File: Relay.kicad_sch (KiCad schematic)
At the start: 6 parts, among them K1 Relay_SPST-NO, Q1 AO3400A

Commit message: more schematic work and initial layout
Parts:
- removed D16: D_Schottky, Diode_SMD:D_SMA, symbol Device:D_Schottky
- removed K1: Relay_SPST-NO, Relay_THT:Relay_SPST_SANYOU_SRD_Series_Form_A, symbol Relay:Relay_SPST-NO
- added D18: D_Schottky, Diode_SMD:D_SOD-123F, symbol Device:D_Schottky
- added K2: SANYOU_SRD_Form_A, Relay_THT:Relay_SPST_SANYOU_SRD_Series_Form_A, symbol Relay:SANYOU_SRD_Form_A
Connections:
- net +5V: now also D18.1 (K), K2.2
- net SW1: now also K2.3
- net SW2: now also K2.1
- net at Q1.3 (D): now also D18.2 (A), K2.5
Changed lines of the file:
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@@
 	(paper "A4")
+	(junction
+		(at 139.7 101.6)
+		(diameter 0)
+		(color 0 0 0 0)
+	)
 	(junction
 		(at 110.49 124.46)
@@
 	)
 	(junction
-		(at 154.94 101.6)
-		(diameter 0)
-		(color 0 0 0 0)
-	)
-	(junction
 		(at 121.92 124.46)
 		(diameter 0)
@@
 	)
 	(junction
-		(at 110.49 109.22)
+		(at 154.94 101.6)
 		(diameter 0)
 		(color 0 0 0 0)
 	)
 	(junction
-		(at 139.7 101.6)
+		(at 110.49 109.22)
 		(diameter 0)
 		(color 0 0 0 0)
@@
 	(hierarchical_label "SW1"
 		(shape passive)
-		(at 139.7 88.9 180)
+		(at 139.7 91.44 180)
 		(effects
 			(font
@@
 		)
 		(instances
-			(project "RSC-LV3-BPS"
+			(project "RSC-LV3-LVBPS"
 				(path "/4bbf2fff-9f66-421d-84bf-68d1dcd1e11d/99b902d4-84f6-4664-999c-14b01031412b"
 					(reference "D23")
@@
 		)
 		(instances
-			(project "RSC-LV3-BPS"
+			(project "RSC-LV3-LVBPS"
 				(path "/4bbf2fff-9f66-421d-84bf-68d1dcd1e11d/99b902d4-84f6-4664-999c-14b01031412b"
 					(reference "R29")
@@
 				(path "/4bbf2fff-9f66-421d-84bf-68d1dcd1e11d/df7bcb64-4221-4af7-8ca5-3f00264c9667"
 					(reference "R28")
-					(unit 1)
-				)
-			)
-		)
-	)
-	(symbol
-		(lib_id "Relay:Relay_SPST-NO")
-		(at 147.32 96.52 90)
-		(unit 1)
-		(body_style 1)
-		(exclude_from_sim no)
-		(in_bom yes)
-		(on_board yes)
-		(in_pos_files yes)
-		(dnp no)
-		(fields_autoplaced yes)
-		(property "Reference" "K1"
-			(at 147.32 81.28 90)
-			(show_name no)
-			(do_not_autoplace no)
-			(effects
-				(font
-					(size 1.27 1.27)
-				)
-			)
-		)
-		(property "Value" "Relay_SPST-NO"
-			(at 147.32 83.82 90)
-			(show_name no)
-			(do_not_autoplace no)
-			(effects
-				(font
-					(size 1.27 1.27)
-				)
-			)
-		)
-		(property "Footprint" "Relay_THT:Relay_SPST_SANYOU_SRD_Series_Form_A"
-			(at 148.59 85.09 0)
-			(hide yes)
-			(show_name no)
-			(do_not_autoplace no)
-			(effects
-				(font
-					(size 1.27 1.27)
-				)
-				(justify left)
-			)
-		)
-		(property "Datasheet" ""
-			(at 147.32 96.52 0)
-			(hide yes)
-			(show_name no)
-			(do_not_autoplace no)
-			(effects
-				(font
-					(size 1.27 1.27)
-				)
-			)
-		)
-		(property "Description" "Relay SPST, normally open, EN50005"
-			(at 147.32 96.52 0)
-			(hide yes)
-			(show_name no)
-			(do_not_autoplace no)
-			(effects
-				(font
-					(size 1.27 1.27)
-				)
-			)
-		)
-		(pin "A2"
-		)
-		(pin "A1"
-		)
-		(pin "14"
-		)
-		(pin "13"
-		)
-		(instances
-			(project "RSC-LV3-BPS"
-				(path "/4bbf2fff-9f66-421d-84bf-68d1dcd1e11d/99b902d4-84f6-4664-999c-14b01031412b"
-					(reference "K3")
-					(unit 1)
-				)
-				(path "/4bbf2fff-9f66-421d-84bf-68d1dcd1e11d/df7bcb64-4221-4af7-8ca5-3f00264c9667"
-					(reference "K1")
 					(unit 1)
 				)
@@
 		(dnp no)
 		(fields_autoplaced yes)
-		(property "Reference" "D16"
+		(property "Reference" "D18"
 			(at 147.6375 111.76 0)
 			(show_name no)
@@
 			)
 		)
-		(property "Footprint" "Diode_SMD:D_SMA"
+		(property "Footprint" "Diode_SMD:D_SOD-123F"
 			(at 147.32 118.11 0)
 			(hide yes)
@@
 		)
 		(instances
-			(project "RSC-LV3-BPS"
+			(project "RSC-LV3-LVBPS"
 				(path "/4bbf2fff-9f66-421d-84bf-68d1dcd1e11d/99b902d4-84f6-4664-999c-14b01031412b"
-					(reference "D17")
+					(reference "D19")
 					(unit 1)
 				)
 				(path "/4bbf2fff-9f66-421d-84bf-68d1dcd1e11d/df7bcb64-4221-4af7-8ca5-3f00264c9667"
-					(reference "D16")
+					(reference "D18")
+					(unit 1)
+				)
+			)
+		)
+	)
+	(symbol
+		(lib_id "Relay:SANYOU_SRD_Form_A")
+		(at 147.32 96.52 90)
+		(unit 1)
+		(body_style 1)
+		(exclude_from_sim no)
+		(in_bom yes)
+		(on_board yes)
+		(in_pos_files yes)
+		(dnp no)
+		(fields_autoplaced yes)
+		(property "Reference" "K2"
+			(at 147.32 83.82 90)
+			(show_name no)
+			(do_not_autoplace no)
+			(effects
+				(font
+					(size 1.27 1.27)
+				)
+			)
+		)
+		(property "Value" "SANYOU_SRD_Form_A"
+			(at 147.32 86.36 90)
+			(show_name no)
+			(do_not_autoplace no)
+			(effects
+				(font
+					(size 1.27 1.27)
+				)
+			)
+		)
+		(property "Footprint" "Relay_THT:Relay_SPST_SANYOU_SRD_Series_Form_A"
+			(at 148.59 87.63 0)
+			(hide yes)
+			(show_name no)
+			(do_not_autoplace no)
+			(effects
+				(font
+					(size 1.27 1.27)
+				)
+				(justify left)
+			)
+		)
+		(property "Datasheet" "http://www.sanyourelay.ca/public/products/pdf/SRD.pdf"
+			(at 147.32 96.52 0)
+			(hide yes)
+			(show_name no)
+			(do_not_autoplace no)
+			(effects
+				(font
+					(size 1.27 1.27)
+				)
+			)
+		)
+		(property "Description" "Sanyo SRD relay, Single Pole Miniature Power Relay, Closing Contact"
+			(at 147.32 96.52 0)
+			(hide yes)
+			(show_name no)
+			(do_not_autoplace no)
+			(effects
+				(font
+					(size 1.27 1.27)
+				)
+			)
+		)
+		(pin "3"
+		)
+		(pin "5"
+		)
+		(pin "1"
+		)
+		(pin "2"
+		)
+		(instances
+			(project "RSC-LV3-LVBPS"
+				(path "/4bbf2fff-9f66-421d-84bf-68d1dcd1e11d/99b902d4-84f6-4664-999c-14b01031412b"
+					(reference "K4")
+					(unit 1)
+				)
+				(path "/4bbf2fff-9f66-421d-84bf-68d1dcd1e11d/df7bcb64-4221-4af7-8ca5-3f00264c9667"
+					(reference "K2")
 					(unit 1)
 				)
@@
 		)
 		(instances
-			(project "RSC-LV3-BPS"
+			(project "RSC-LV3-LVBPS"
 				(path "/4bbf2fff-9f66-421d-84bf-68d1dcd1e11d/99b902d4-84f6-4664-999c-14b01031412b"
 					(reference "#PWR054")
@@
 		)
 		(instances
-			(project "RSC-LV3-BPS"
+			(project "RSC-LV3-LVBPS"
 				(path "/4bbf2fff-9f66-421d-84bf-68d1dcd1e11d/99b902d4-84f6-4664-999c-14b01031412b"
 					(reference "#PWR052")
@@
 		)
 		(instances
-			(project "RSC-LV3-BPS"
+			(project "RSC-LV3-LVBPS"
 				(path "/4bbf2fff-9f66-421d-84bf-68d1dcd1e11d/99b902d4-84f6-4664-999c-14b01031412b"
 					(reference "R42")
@@
 		)
 		(instances
-			(project "RSC-LV3-BPS"
+			(project "RSC-LV3-LVBPS"
 				(path "/4bbf2fff-9f66-421d-84bf-68d1dcd1e11d/99b902d4-84f6-4664-999c-14b01031412b"
 					(reference "Q2")

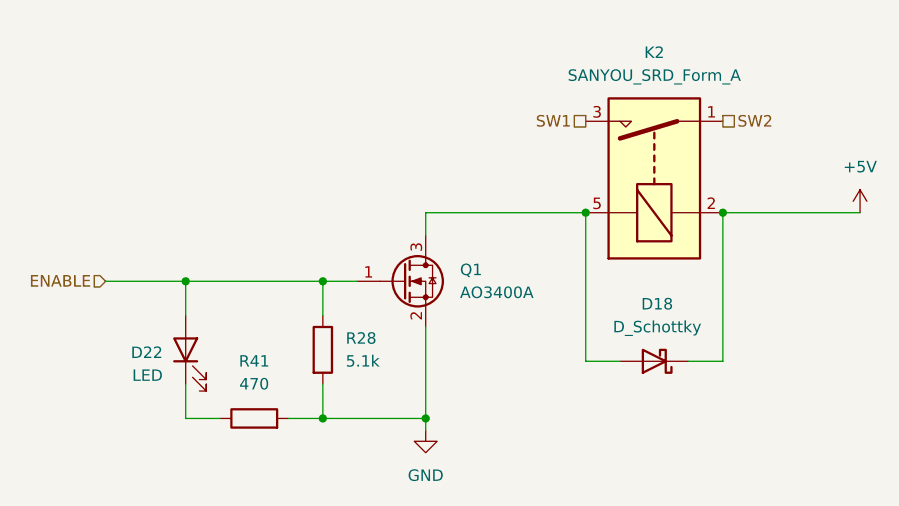
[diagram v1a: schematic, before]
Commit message: finished layout, routing, and silkscreen
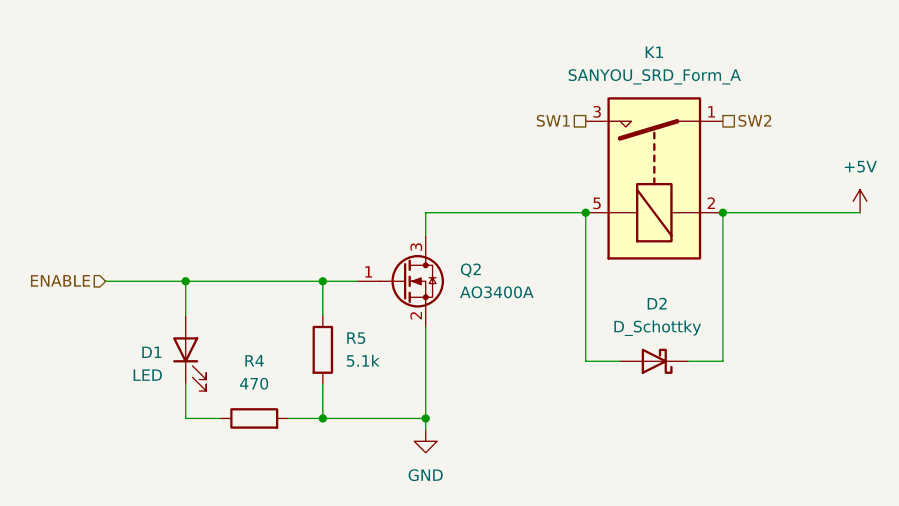
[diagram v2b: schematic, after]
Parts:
- renumbered D22 to D1, D18 to D2, K2 to K1, Q1 to Q2, R41 to R4, R28 to R5
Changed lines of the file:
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@@
 		(dnp no)
 		(fields_autoplaced yes)
-		(property "Reference" "D22"
+		(property "Reference" "D1"
 			(at 92.71 117.1574 90)
 			(show_name no)
@@
 			(project "RSC-LV3-LVBPS"
 				(path "/4bbf2fff-9f66-421d-84bf-68d1dcd1e11d/99b902d4-84f6-4664-999c-14b01031412b"
-					(reference "D23")
-					(unit 1)
-				)
-				(path "/4bbf2fff-9f66-421d-84bf-68d1dcd1e11d/df7bcb64-4221-4af7-8ca5-3f00264c9667"
-					(reference "D22")
+					(reference "D4")
+					(unit 1)
+				)
+				(path "/4bbf2fff-9f66-421d-84bf-68d1dcd1e11d/df7bcb64-4221-4af7-8ca5-3f00264c9667"
+					(reference "D1")
 					(unit 1)
 				)
@@
 		(dnp no)
 		(fields_autoplaced yes)
-		(property "Reference" "R28"
+		(property "Reference" "R5"
 			(at 113.03 115.5699 0)
 			(show_name no)
@@
 			(project "RSC-LV3-LVBPS"
 				(path "/4bbf2fff-9f66-421d-84bf-68d1dcd1e11d/99b902d4-84f6-4664-999c-14b01031412b"
-					(reference "R29")
-					(unit 1)
-				)
-				(path "/4bbf2fff-9f66-421d-84bf-68d1dcd1e11d/df7bcb64-4221-4af7-8ca5-3f00264c9667"
-					(reference "R28")
+					(reference "R11")
+					(unit 1)
+				)
+				(path "/4bbf2fff-9f66-421d-84bf-68d1dcd1e11d/df7bcb64-4221-4af7-8ca5-3f00264c9667"
+					(reference "R5")
 					(unit 1)
 				)
@@
 		(dnp no)
 		(fields_autoplaced yes)
-		(property "Reference" "D18"
+		(property "Reference" "D2"
 			(at 147.6375 111.76 0)
 			(show_name no)
@@
 			(project "RSC-LV3-LVBPS"
 				(path "/4bbf2fff-9f66-421d-84bf-68d1dcd1e11d/99b902d4-84f6-4664-999c-14b01031412b"
-					(reference "D19")
-					(unit 1)
-				)
-				(path "/4bbf2fff-9f66-421d-84bf-68d1dcd1e11d/df7bcb64-4221-4af7-8ca5-3f00264c9667"
-					(reference "D18")
+					(reference "D5")
+					(unit 1)
+				)
+				(path "/4bbf2fff-9f66-421d-84bf-68d1dcd1e11d/df7bcb64-4221-4af7-8ca5-3f00264c9667"
+					(reference "D2")
 					(unit 1)
 				)
@@
 		(dnp no)
 		(fields_autoplaced yes)
-		(property "Reference" "K2"
+		(property "Reference" "K1"
 			(at 147.32 83.82 90)
 			(show_name no)
@@
 			(project "RSC-LV3-LVBPS"
 				(path "/4bbf2fff-9f66-421d-84bf-68d1dcd1e11d/99b902d4-84f6-4664-999c-14b01031412b"
-					(reference "K4")
-					(unit 1)
-				)
-				(path "/4bbf2fff-9f66-421d-84bf-68d1dcd1e11d/df7bcb64-4221-4af7-8ca5-3f00264c9667"
 					(reference "K2")
+					(unit 1)
+				)
+				(path "/4bbf2fff-9f66-421d-84bf-68d1dcd1e11d/df7bcb64-4221-4af7-8ca5-3f00264c9667"
+					(reference "K1")
 					(unit 1)
 				)
@@
 		(dnp no)
 		(fields_autoplaced yes)
-		(property "Reference" "#PWR053"
+		(property "Reference" "#PWR012"
 			(at 170.18 105.41 0)
 			(hide yes)
@@
 			(project "RSC-LV3-LVBPS"
 				(path "/4bbf2fff-9f66-421d-84bf-68d1dcd1e11d/99b902d4-84f6-4664-999c-14b01031412b"
-					(reference "#PWR054")
-					(unit 1)
-				)
-				(path "/4bbf2fff-9f66-421d-84bf-68d1dcd1e11d/df7bcb64-4221-4af7-8ca5-3f00264c9667"
-					(reference "#PWR053")
+					(reference "#PWR021")
+					(unit 1)
+				)
+				(path "/4bbf2fff-9f66-421d-84bf-68d1dcd1e11d/df7bcb64-4221-4af7-8ca5-3f00264c9667"
+					(reference "#PWR012")
 					(unit 1)
 				)
@@
 		(dnp no)
 		(fields_autoplaced yes)
-		(property "Reference" "#PWR051"
+		(property "Reference" "#PWR011"
 			(at 121.92 132.08 0)
 			(hide yes)
@@
 			(project "RSC-LV3-LVBPS"
 				(path "/4bbf2fff-9f66-421d-84bf-68d1dcd1e11d/99b902d4-84f6-4664-999c-14b01031412b"
-					(reference "#PWR052")
-					(unit 1)
-				)
-				(path "/4bbf2fff-9f66-421d-84bf-68d1dcd1e11d/df7bcb64-4221-4af7-8ca5-3f00264c9667"
-					(reference "#PWR051")
+					(reference "#PWR020")
+					(unit 1)
+				)
+				(path "/4bbf2fff-9f66-421d-84bf-68d1dcd1e11d/df7bcb64-4221-4af7-8ca5-3f00264c9667"
+					(reference "#PWR011")
 					(unit 1)
 				)
@@
 		(dnp no)
 		(fields_autoplaced yes)
-		(property "Reference" "R41"
+		(property "Reference" "R4"
 			(at 102.87 118.11 90)
 			(show_name no)
@@
 			(project "RSC-LV3-LVBPS"
 				(path "/4bbf2fff-9f66-421d-84bf-68d1dcd1e11d/99b902d4-84f6-4664-999c-14b01031412b"
-					(reference "R42")
-					(unit 1)
-				)
-				(path "/4bbf2fff-9f66-421d-84bf-68d1dcd1e11d/df7bcb64-4221-4af7-8ca5-3f00264c9667"
-					(reference "R41")
+					(reference "R10")
+					(unit 1)
+				)
+				(path "/4bbf2fff-9f66-421d-84bf-68d1dcd1e11d/df7bcb64-4221-4af7-8ca5-3f00264c9667"
+					(reference "R4")
 					(unit 1)
 				)
@@
 		(dnp no)
 		(fields_autoplaced yes)
-		(property "Reference" "Q1"
+		(property "Reference" "Q2"
 			(at 125.73 107.9499 0)
 			(show_name no)
@@
 			(project "RSC-LV3-LVBPS"
 				(path "/4bbf2fff-9f66-421d-84bf-68d1dcd1e11d/99b902d4-84f6-4664-999c-14b01031412b"
+					(reference "Q3")
+					(unit 1)
+				)
+				(path "/4bbf2fff-9f66-421d-84bf-68d1dcd1e11d/df7bcb64-4221-4af7-8ca5-3f00264c9667"
 					(reference "Q2")
 					(unit 1)
 				)
-				(path "/4bbf2fff-9f66-421d-84bf-68d1dcd1e11d/df7bcb64-4221-4af7-8ca5-3f00264c9667"
-					(reference "Q1")
-					(unit 1)
-				)
